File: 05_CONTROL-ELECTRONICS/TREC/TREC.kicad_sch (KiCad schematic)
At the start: 2 parts, among them U1 STM32F401RETx, U2 DRV8301DCA

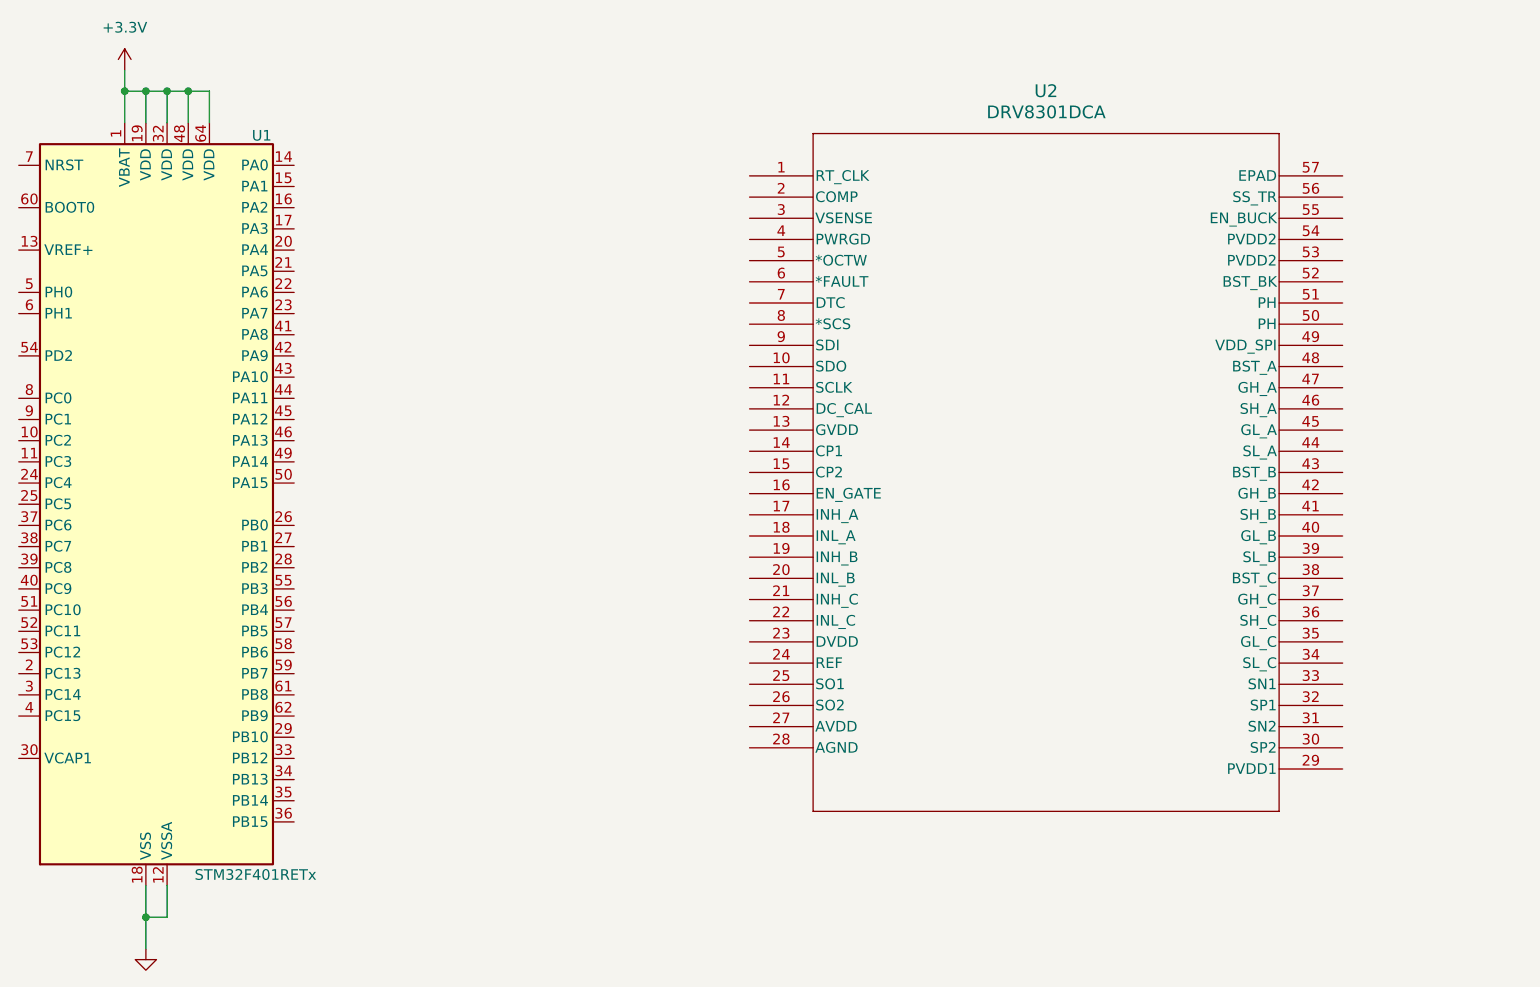
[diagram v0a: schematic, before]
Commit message: TREC schematic - added capacitors for decoup + volt reg
Cleaned up the schematic for TREC by diving into MCU and including a pinout image and using datasheet with Phil's lab udemy course to include capacitors for decoupling, analog decoupling, and voltage regulation.
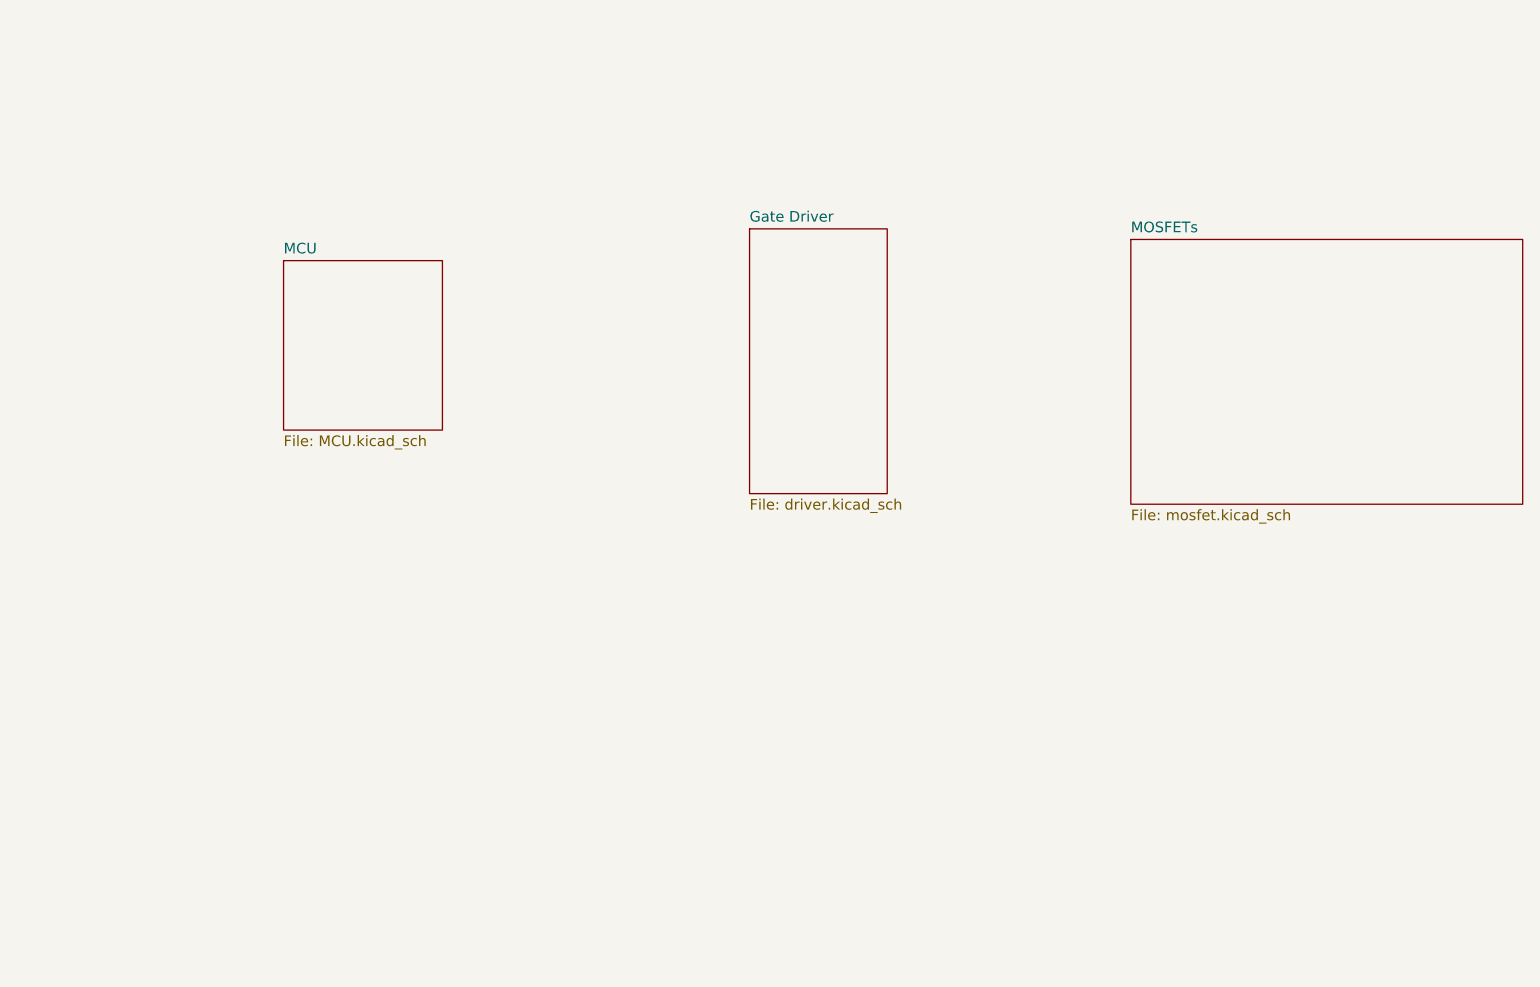
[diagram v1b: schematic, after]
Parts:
- removed U1: STM32F401RETx, Package_QFP:LQFP-64_10x10mm_P0.5mm, symbol MCU_ST_STM32F4:STM32F401RETx
- removed U2: DRV8301DCA, DCA56_6P35X3P61, symbol 2024-08-26_19-09-43:DRV8301DCA
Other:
- added sheet Gate Driver (driver.kicad_sch)
- added sheet MCU (MCU.kicad_sch)
- added sheet MOSFETs (mosfet.kicad_sch)
